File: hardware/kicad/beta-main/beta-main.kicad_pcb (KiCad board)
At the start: 4 copper layers, 0 parts

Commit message: create template for components placement with drawn contraints
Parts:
- added C1: 220u, Capacitor_SMD:C_1210_3225Metric, F.Cu at (254.0, 98.5)
- added C10: 22u, Capacitor_SMD:C_0805_2012Metric, F.Cu at (211.2, 106.2)
- added C11: 22u, Capacitor_SMD:C_0805_2012Metric, F.Cu at (211.2, 109.2)
- added C12: 10u, Capacitor_SMD:C_0805_2012Metric, F.Cu at (196.8, 94.2)
- added C13: 10u, Capacitor_SMD:C_0805_2012Metric, F.Cu at (196.8, 97.2)
- added C14: 0.1u, Capacitor_SMD:C_0402_1005Metric, F.Cu at (203.3, 104.4)
- added C15: 4.7nF, Capacitor_SMD:C_0402_1005Metric, F.Cu at (203.3, 106.3)
- added C16: 10u, Capacitor_SMD:C_0805_2012Metric, F.Cu at (196.8, 100.2)
- added C17: 10u, Capacitor_SMD:C_0805_2012Metric, F.Cu at (196.8, 103.2)
- added C18: 10u, Capacitor_SMD:C_0805_2012Metric, F.Cu at (196.8, 106.2)
- added C19: 10u, Capacitor_SMD:C_0805_2012Metric, F.Cu at (196.8, 109.2)
- added C2: 0.1u, Capacitor_SMD:C_0603_1608Metric_Pad1.08x0.95mm_HandSolder, F.Cu at (225.7, 99.6)
- added C5: 10u, Capacitor_SMD:C_0805_2012Metric, F.Cu at (211.2, 94.2)
- added C6: 10u, Capacitor_SMD:C_0805_2012Metric, F.Cu at (211.2, 97.2)
- added C7: 0.1u, Capacitor_SMD:C_0402_1005Metric, F.Cu at (214.9, 107.4)
- added C8: 22u, Capacitor_SMD:C_0805_2012Metric, F.Cu at (211.2, 100.2)
- added C9: 22u, Capacitor_SMD:C_0805_2012Metric, F.Cu at (211.2, 103.2)
- added F1: 10A, Fuse:Fuse_1206_3216Metric, F.Cu at (259.6, 98.0)
- added FID1: ~, Fiducial:Fiducial_1mm_Mask2mm, F.Cu at (247.4, 66.2)
- added FID2: ~, Fiducial:Fiducial_1mm_Mask2mm, F.Cu at (247.4, 69.8)
- added FID3: ~, Fiducial:Fiducial_1mm_Mask2mm, F.Cu at (247.4, 73.3)
- added J1: FFC3A20-15-G, Connector_FFC-FPC:TE_1-84953-5_1x15-1MP_P1.0mm_Horizontal, F.Cu at (127.2, 100.0)
- added J10: Servo Socket, Connector_PinHeader_2.54mm:PinHeader_1x03_P2.54mm_Vertical, F.Cu at (258.0, 66.8)
- added J11: Servo Socket, Connector_PinHeader_2.54mm:PinHeader_1x03_P2.54mm_Vertical, F.Cu at (262.6, 66.8)
- added J12: Servo Socket, Connector_PinHeader_2.54mm:PinHeader_1x03_P2.54mm_Vertical, F.Cu at (267.2, 66.8)
- added J2: FFC3A20-15-G, Connector_FFC-FPC:TE_1-84953-5_1x15-1MP_P1.0mm_Horizontal, F.Cu at (100.0, 50.2)
- added J3: XT60, Connector_AMASS:AMASS_XT60-F_1x02_P7.20mm_Vertical, F.Cu at (256.3, 91.2)
- added J8: Conn_01x02_Socket, Connector_PinHeader_2.54mm:PinHeader_1x02_P2.54mm_Vertical, F.Cu at (264.9, 36.8)
- added J9: Servo Socket, Connector_PinHeader_2.54mm:PinHeader_1x03_P2.54mm_Vertical, F.Cu at (253.4, 66.8)
- added L1: 2.2u, Inductor_SMD:L_Bourns_SRP5030T, F.Cu at (217.5, 96.0)
- added L2: 2.2u, CM5IO:L_Bourns_SRP5030CC, F.Cu at (203.0, 96.3)
- added MH1: M3, MountingHole:MountingHole_3.2mm_M3_Pad_Via, F.Cu at (66.0, 43.5)
- added MH2: M3, MountingHole:MountingHole_3.2mm_M3_Pad_Via, F.Cu at (134.0, 43.5)
- added MH3: M3, MountingHole:MountingHole_3.2mm_M3_Pad_Via, F.Cu at (66.0, 156.5)
- added MH4: M3, MountingHole:MountingHole_3.2mm_M3_Pad_Via, F.Cu at (134.0, 156.5)
- added Module1: ComputeModule5-CM5, CM5IO:Raspberry-Pi-5-Compute-Module, F.Cu at (83.5, 124.0)
- added Q2: MMBT3906, Package_TO_SOT_SMD:SOT-23, F.Cu at (261.7, 76.4)
- added R1: 220K, Resistor_SMD:R_0402_1005Metric, F.Cu at (214.9, 100.4)
- added R11: 20k, Resistor_SMD:R_0402_1005Metric, F.Cu at (252.6, 75.1)
- added R12: 10k, Resistor_SMD:R_0402_1005Metric, F.Cu at (252.6, 77.1)
- added R13: 10k, Resistor_SMD:R_0402_1005Metric, F.Cu at (252.6, 79.1)
- added R14: 10k, Resistor_SMD:R_0402_1005Metric, F.Cu at (252.6, 81.1)
- added R15: 10k, Resistor_SMD:R_0402_1005Metric, F.Cu at (252.6, 83.1)
- added R2: 30K, Resistor_SMD:R_0402_1005Metric, F.Cu at (214.9, 102.4)
- added R3: 100K 1%, Resistor_SMD:R_0402_1005Metric, F.Cu at (200.4, 100.7)
- added R4: 10K 1%, Resistor_SMD:R_0402_1005Metric, F.Cu at (200.4, 102.7)
- added R5: 2.2K 1%, Resistor_SMD:R_0402_1005Metric, F.Cu at (200.4, 104.7)
- added TP1: 5V, TestPoint:TestPoint_Pad_D1.0mm, F.Cu at (215.0, 104.9)
- added U1: MAX98357A, Package_DFN_QFN:TQFN-16-1EP_3x3mm_P0.5mm_EP1.23x1.23mm, F.Cu at (240.7, 59.9)
- added U2: TPS56624x, Package_TO_SOT_SMD:SOT-563, F.Cu at (218.1, 101.1)
- added U3: AP3441SHE-7B, Package_DFN_QFN:DFN-8-1EP_2x2mm_P0.5mm_EP1.05x1.75mm, F.Cu at (204.1, 101.6)
- added U6: BNO086, BNO086:IC_BNO086, F.Cu at (226.9, 95.6)
- added U7: 74LVC1G126, Package_TO_SOT_SMD:SOT-23-5, F.Cu at (256.6, 76.5)
- added U8: 74LVC1G126, Package_TO_SOT_SMD:SOT-23-5, F.Cu at (256.6, 81.2)
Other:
- board outline added: 76 x 121 mm
- board text added: "Display"

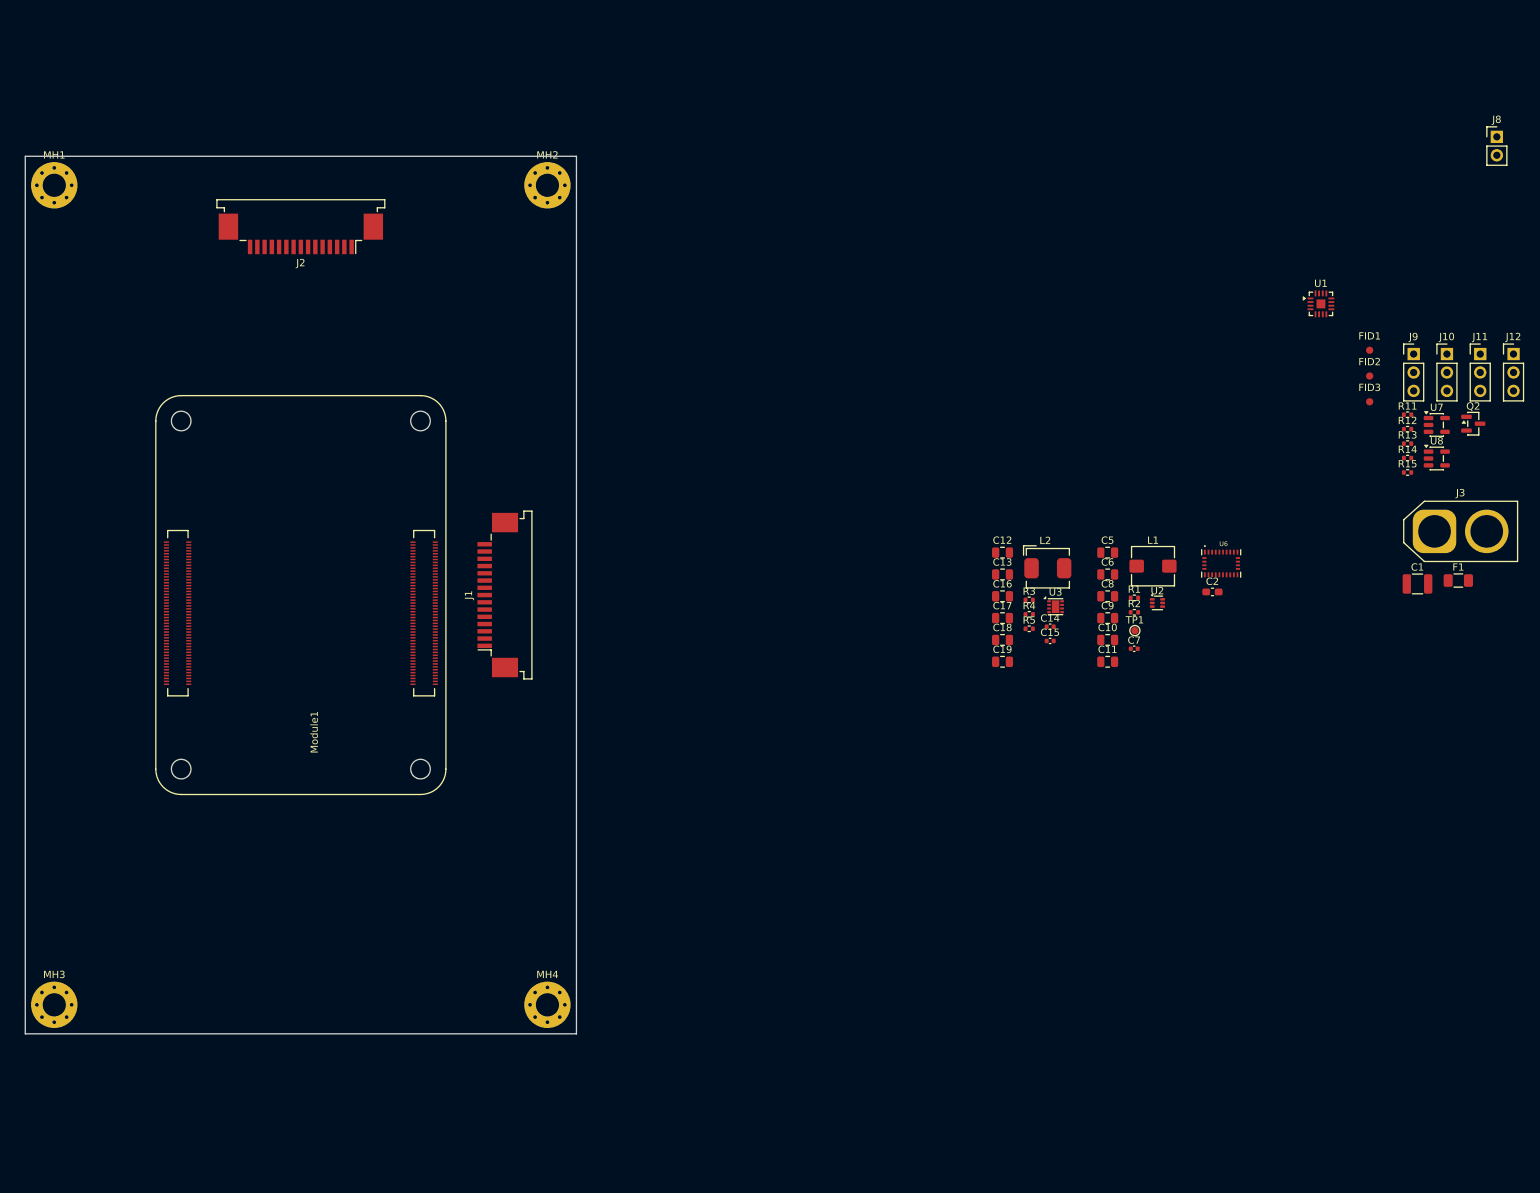
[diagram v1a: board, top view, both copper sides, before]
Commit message: Rough layout with all elements, test point for 3V3 added. C footprints need to change to 6 3
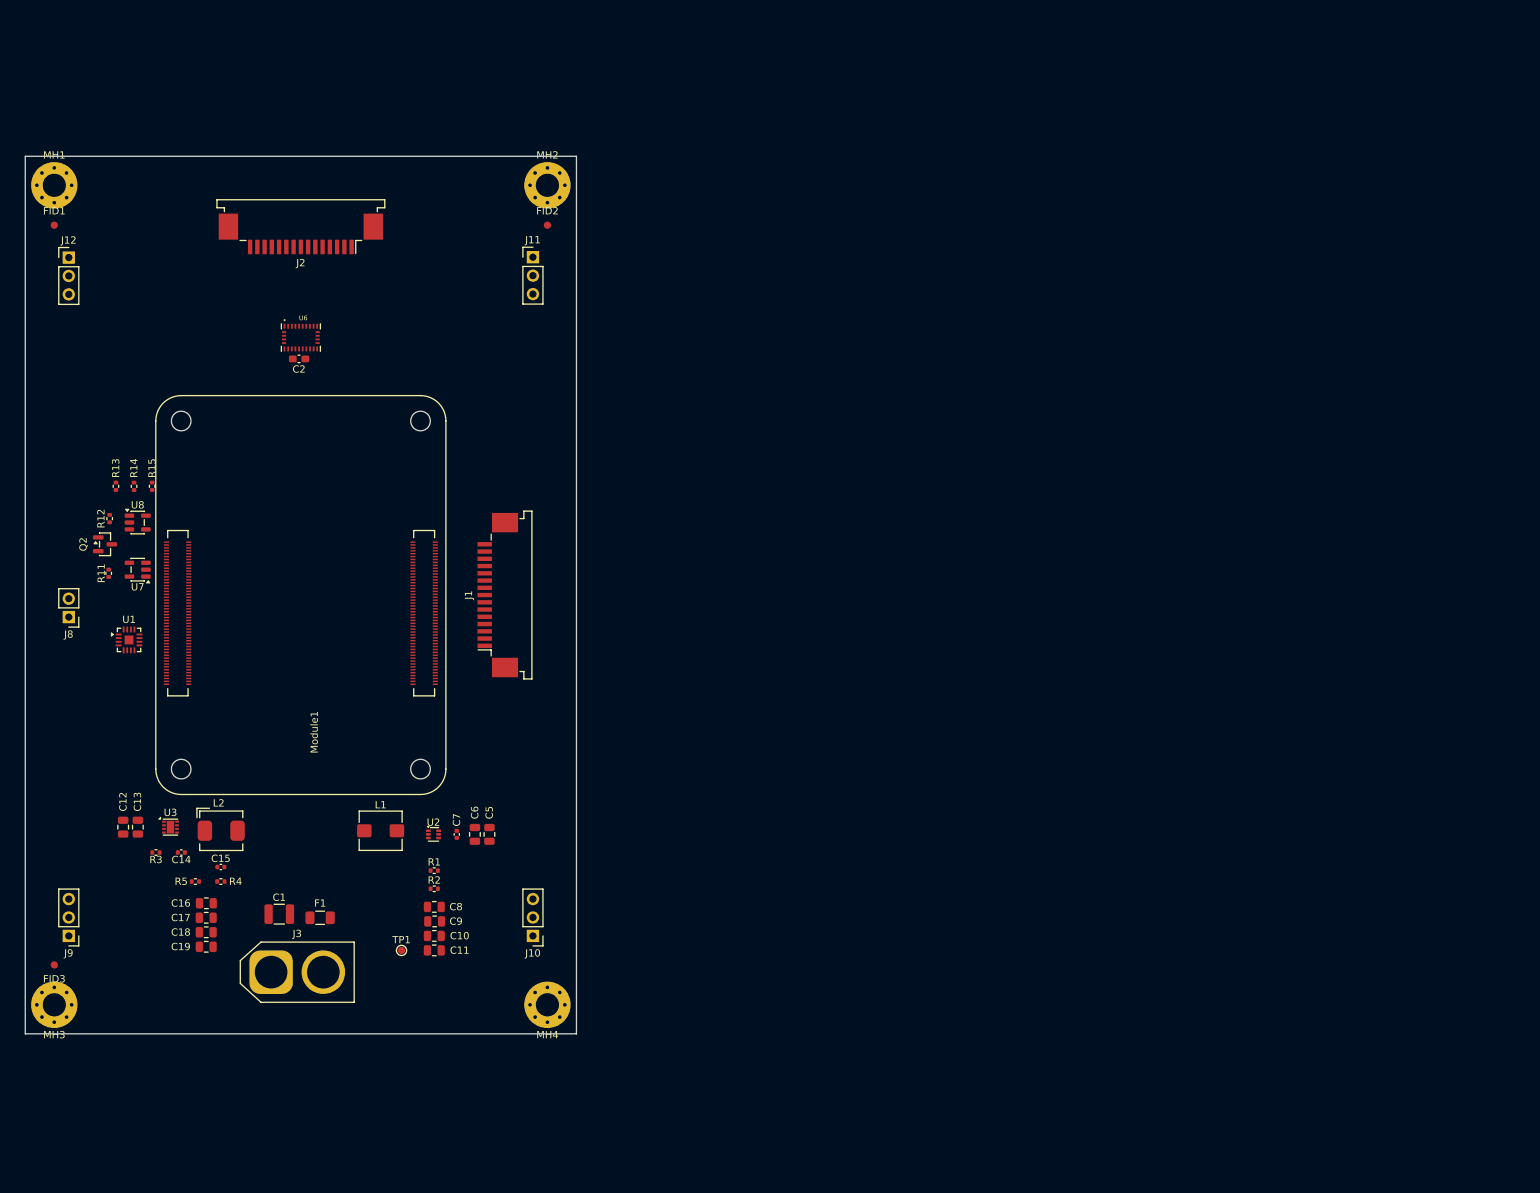
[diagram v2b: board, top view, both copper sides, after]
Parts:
- moved J8 207.7 mm to (68.0, 103.0), turned to 180 degrees
- moved J9 202.1 mm to (68.0, 147.0), turned to 180 degrees
- moved J12 199.7 mm to (68.0, 53.5)
- moved FID3 197.3 mm to (66.0, 151.0), turned to 180 degrees
- moved Q2 189.4 mm to (73.0, 93.0)
- moved FID1 182.2 mm to (66.0, 49.0)
- moved R11 180.4 mm to (73.5, 97.0), turned to -90 degrees
- moved U7 180.2 mm to (77.5, 96.5), turned to 180 degrees
- moved R12 179.4 mm to (73.6, 89.5), turned to 90 degrees
- moved U8 179.3 mm to (77.5, 90.0)
- moved R13 178.2 mm to (74.5, 85.0), turned to -90 degrees
- moved R14 175.6 mm to (77.0, 85.0), turned to -90 degrees
- moved R15 173.1 mm to (79.5, 85.0), turned to -90 degrees
- moved J3 171.5 mm to (95.9, 152.0)
- moved U1 170.8 mm to (76.3, 106.2)
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
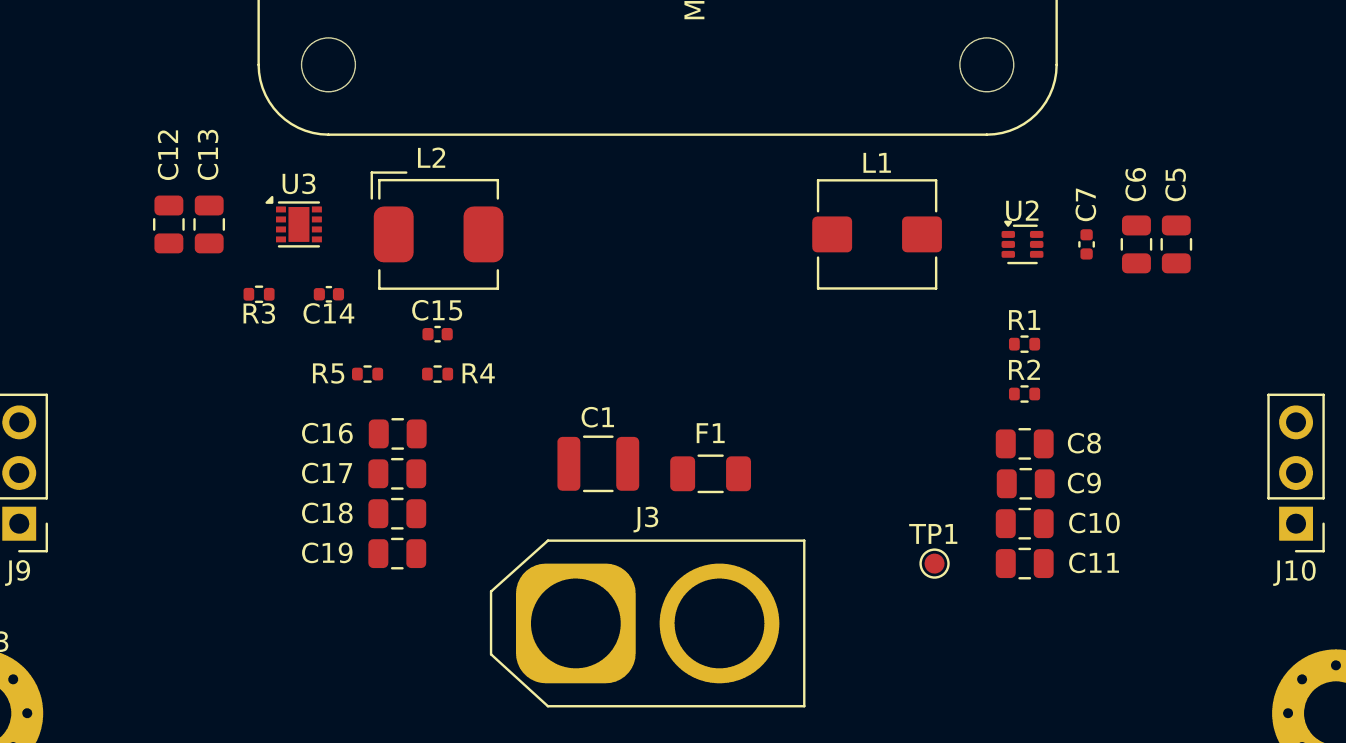
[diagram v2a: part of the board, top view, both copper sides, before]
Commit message: Footprints changed to 603
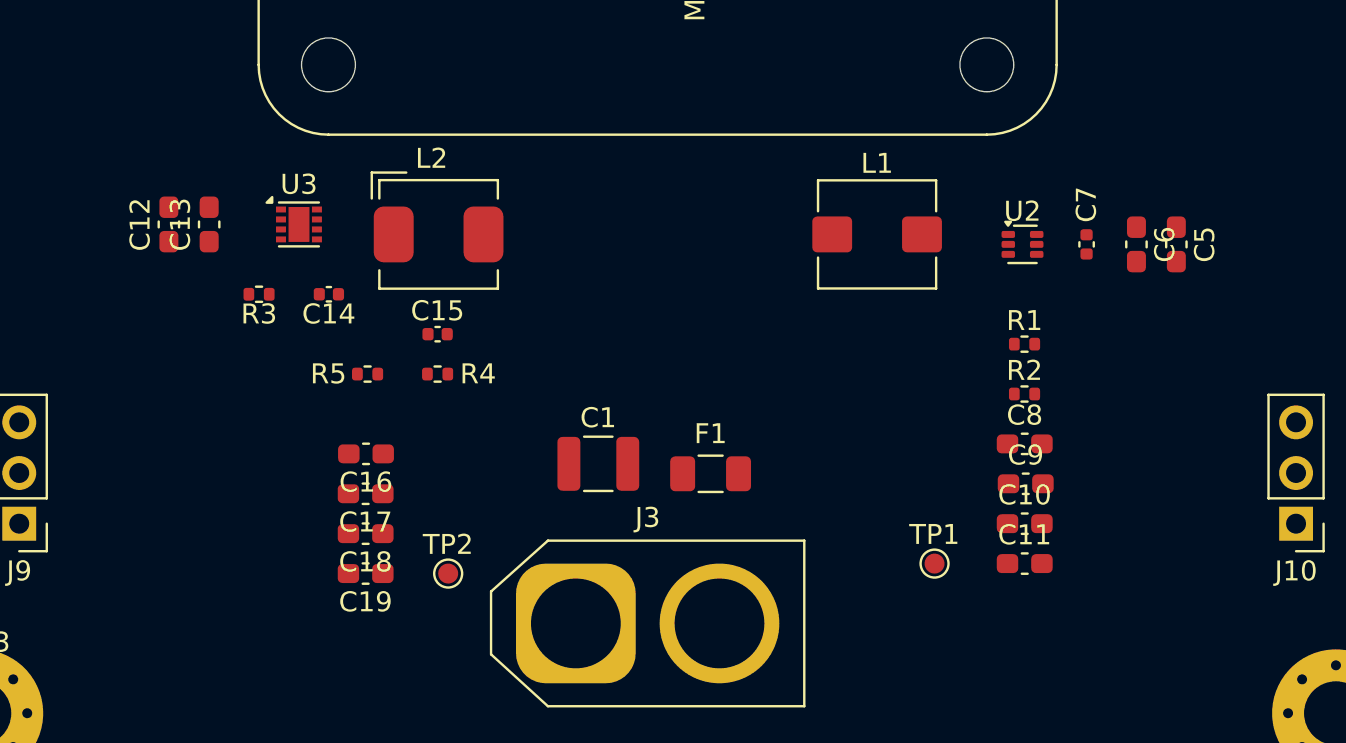
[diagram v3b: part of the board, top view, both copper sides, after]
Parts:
- added TP2: 3V3, TestPoint:TestPoint_Pad_D1.0mm, F.Cu at (89.5, 149.5)
- C10, C11, C12, C13, C16, C17, C18, C19, C5, C6, C8, C9: footprint Capacitor_SMD:C_0805_2012Metric -> Capacitor_SMD:C_0603_1608Metric_Pad1.08x0.95mm_HandSolder
- moved C16 1.88 mm to (85.4, 143.5)
- moved C17 1.88 mm to (85.4, 145.5)
- moved C18 1.88 mm to (85.4, 147.5)
- moved C19 1.88 mm to (85.4, 149.5)

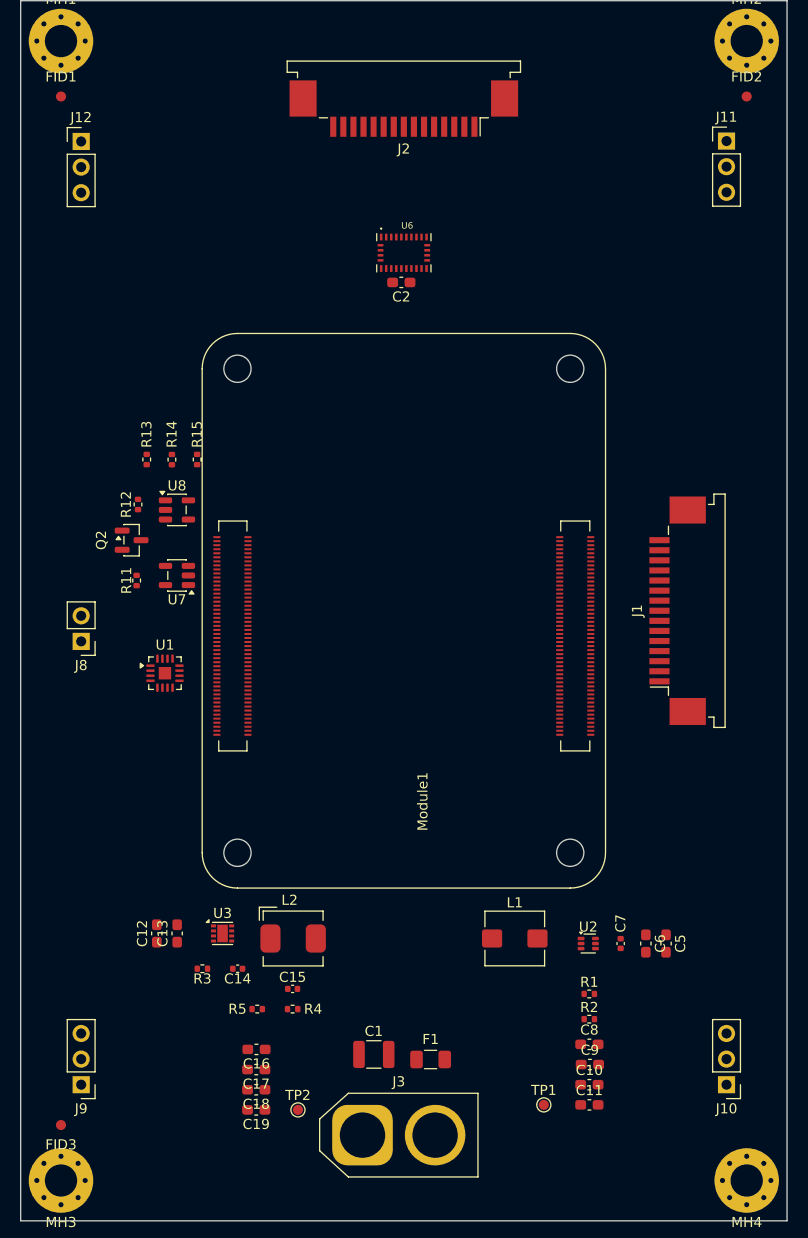
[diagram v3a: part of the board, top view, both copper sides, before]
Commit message: Footprints fixed, fuse removed
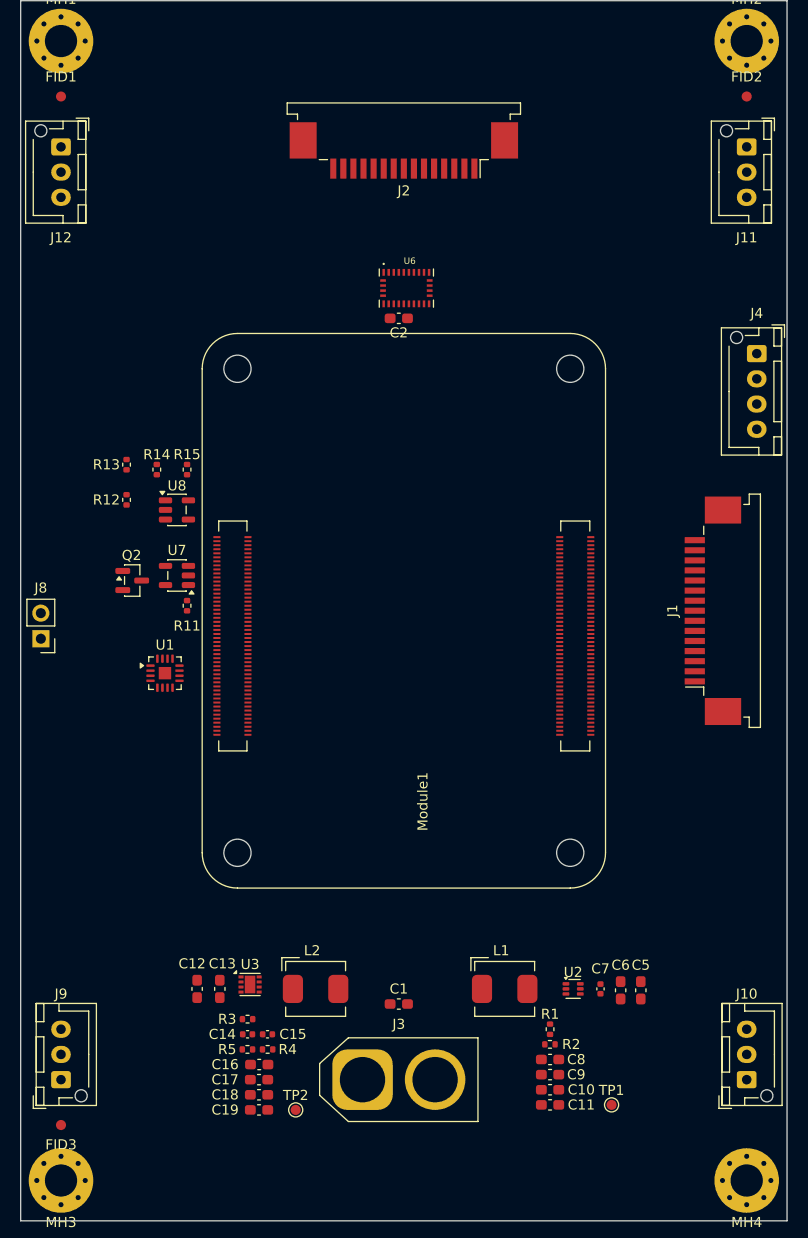
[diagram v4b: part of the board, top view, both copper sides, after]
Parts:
- removed F1: 10A, Fuse:Fuse_1206_3216Metric
- added J4: Conn_01x04_Pin, Connector_JST:JST_XH_B4B-XH-AM_1x04_P2.50mm_Vertical, F.Cu at (135.0, 74.5)
- C1: footprint Capacitor_SMD:C_1210_3225Metric -> Capacitor_SMD:C_0603_1608Metric_Pad1.08x0.95mm_HandSolder
- J10, J11, J12, J9: footprint Connector_PinHeader_2.54mm:PinHeader_1x03_P2.54mm_Vertical -> Connector_JST:JST_XH_B3B-XH-AM_1x03_P2.50mm_Vertical
- L1: footprint Inductor_SMD:L_Bourns_SRP5030T -> CM5IO:L_Bourns_SRP5030CC
- moved C13 6.94 mm to (81.8, 137.5), turned to -90 degrees
- moved C12 6.80 mm to (79.5, 137.5), turned to -90 degrees
- moved TP1 6.72 mm to (120.6, 149.0)
- moved R3 6.71 mm to (84.5, 140.5)
- moved C14 6.57 mm to (84.5, 142.0)
- moved U3 5.75 mm to (84.8, 137.1)
- moved R11 5.59 mm to (78.5, 99.5), turned to 90 degrees
- moved C1 5.58 mm to (99.5, 139.0), turned to 180 degrees
- moved J3 5.50 mm to (95.9, 146.5)
- moved L2 5.47 mm to (91.2, 137.5)
- moved C5 5.27 mm to (123.5, 137.6)
- moved C6 5.27 mm to (121.5, 137.6)
- moved R1 5.23 mm to (114.5, 141.5), turned to 90 degrees
- moved C15 5.14 mm to (86.5, 142.0)
- moved L1 5.10 mm to (110.0, 137.5)
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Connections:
- J3 pad 2: Net-(J3-Pin_2) -> +BATT
